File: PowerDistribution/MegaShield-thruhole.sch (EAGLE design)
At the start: 39 parts, among them IC1 TLE5205-2, IC2 TLE5205-2, IC3 TLE5205-2, J10 DCJ0202

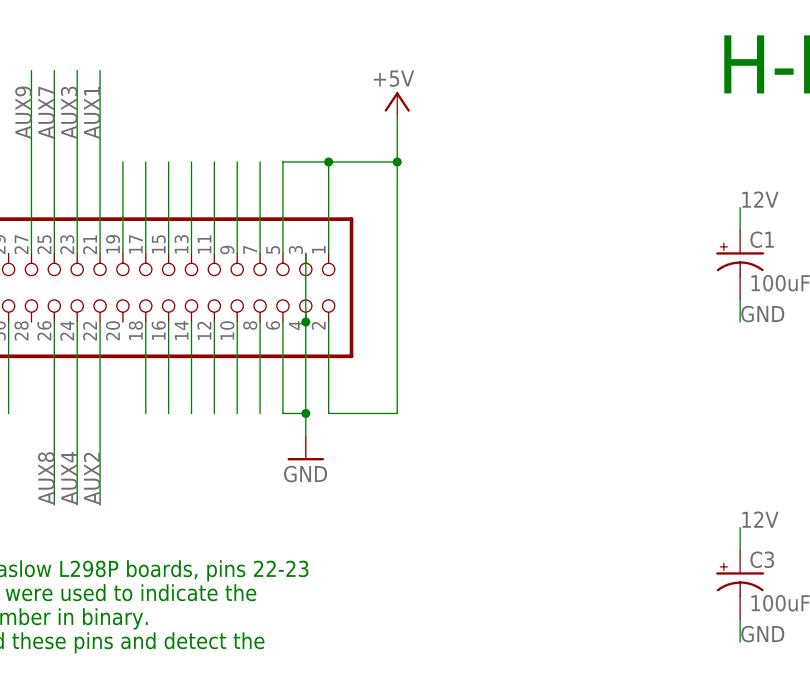
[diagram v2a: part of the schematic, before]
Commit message: Add second 5V bypass cap
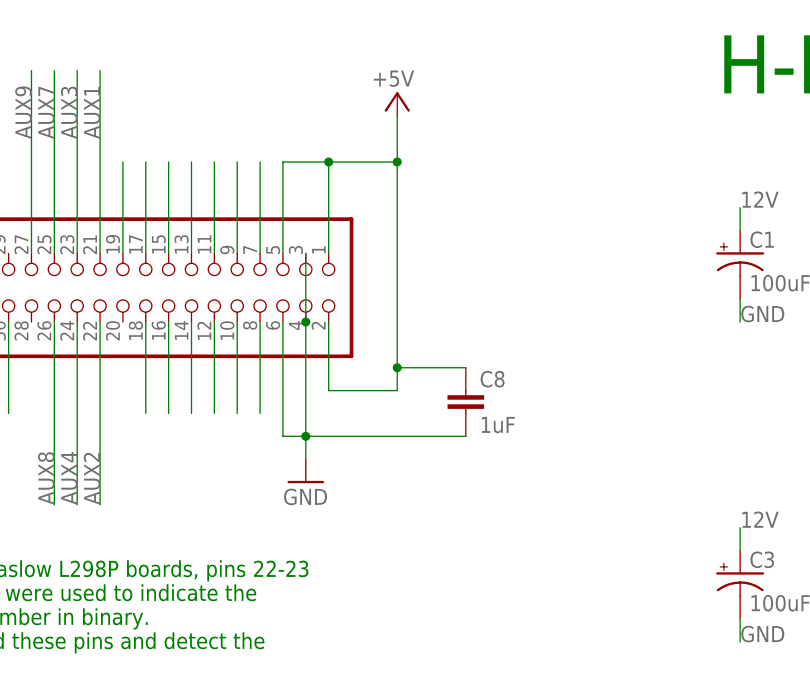
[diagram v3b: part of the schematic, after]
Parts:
- added C8: 1uF, SparkFun:CAPPTH
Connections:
- net 5V: now also C8.1
- net GND: now also C8.2
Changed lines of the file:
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@@
 <part name="GND2" library="supply1" deviceset="GND" device=""/>
 <part name="C7" library="SparkFun" deviceset="CAP" device="PTH" value="1uF"/>
+<part name="C8" library="SparkFun" deviceset="CAP" device="PTH" value="1uF"/>
 </parts>
 <sheets>
@@
 <attribute name="NAME" x="52.07" y="227.584" size="1.778" layer="95" rot="MR0"/>
 </instance>
-<instance part="GND1" gate="1" x="106.68" y="116.84" smashed="yes">
-<attribute name="VALUE" x="104.14" y="114.3" size="1.778" layer="96"/>
+<instance part="GND1" gate="1" x="106.68" y="114.3" smashed="yes">
+<attribute name="VALUE" x="104.14" y="111.76" size="1.778" layer="96"/>
 </instance>
 <instance part="TP1" gate="1" x="160.02" y="180.34"/>
@@
 </instance>
 <instance part="C7" gate="G$1" x="20.32" y="236.22" rot="MR0"/>
+<instance part="C8" gate="G$1" x="124.46" y="121.92"/>
 </instances>
 <busses>
@@
 <wire x1="106.68" y1="139.7" x2="106.68" y2="132.08" width="0.1524" layer="91"/>
 <pinref part="GND1" gate="1" pin="GND"/>
-<wire x1="106.68" y1="119.38" x2="106.68" y2="121.92" width="0.1524" layer="91"/>
-<wire x1="106.68" y1="132.08" x2="106.68" y2="121.92" width="0.1524" layer="91"/>
-<wire x1="106.68" y1="121.92" x2="104.14" y2="121.92" width="0.1524" layer="91"/>
+<wire x1="106.68" y1="116.84" x2="106.68" y2="119.38" width="0.1524" layer="91"/>
+<wire x1="106.68" y1="132.08" x2="106.68" y2="119.38" width="0.1524" layer="91"/>
+<wire x1="106.68" y1="119.38" x2="104.14" y2="119.38" width="0.1524" layer="91"/>
 <pinref part="XIO" gate="A" pin="6"/>
-<wire x1="104.14" y1="121.92" x2="104.14" y2="132.08" width="0.1524" layer="91"/>
-<junction x="106.68" y="121.92"/>
+<wire x1="104.14" y1="119.38" x2="104.14" y2="132.08" width="0.1524" layer="91"/>
+<junction x="106.68" y="119.38"/>
 <junction x="106.68" y="132.08"/>
+<pinref part="C8" gate="G$1" pin="2"/>
+<wire x1="106.68" y1="119.38" x2="124.46" y2="119.38" width="0.1524" layer="91"/>
 </segment>
 </net>
@@
 </segment>
 <segment>
-<wire x1="109.22" y1="132.08" x2="109.22" y2="121.92" width="0.1524" layer="91"/>
-<wire x1="109.22" y1="121.92" x2="116.84" y2="121.92" width="0.1524" layer="91"/>
-<wire x1="116.84" y1="121.92" x2="116.84" y2="149.86" width="0.1524" layer="91"/>
+<wire x1="109.22" y1="132.08" x2="109.22" y2="124.46" width="0.1524" layer="91"/>
+<wire x1="109.22" y1="124.46" x2="116.84" y2="124.46" width="0.1524" layer="91"/>
+<wire x1="116.84" y1="124.46" x2="116.84" y2="127" width="0.1524" layer="91"/>
+<wire x1="116.84" y1="127" x2="116.84" y2="149.86" width="0.1524" layer="91"/>
 <wire x1="116.84" y1="149.86" x2="109.22" y2="149.86" width="0.1524" layer="91"/>
 <wire x1="109.22" y1="149.86" x2="109.22" y2="139.7" width="0.1524" layer="91"/>
@@
 <wire x1="104.14" y1="149.86" x2="109.22" y2="149.86" width="0.1524" layer="91"/>
 <junction x="109.22" y="149.86"/>
-</segment>
-<segment>
+<pinref part="C8" gate="G$1" pin="1"/>
+<wire x1="124.46" y1="127" x2="116.84" y2="127" width="0.1524" layer="91"/>
+<junction x="116.84" y="127"/>
+</segment>
+<segment>

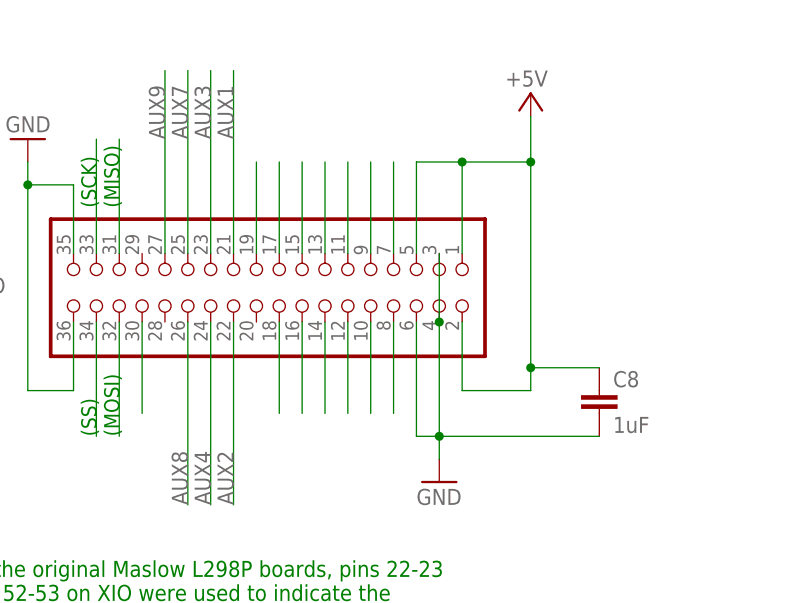
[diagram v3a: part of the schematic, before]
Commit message: Move caps on schematic, change colors in SMD .brd
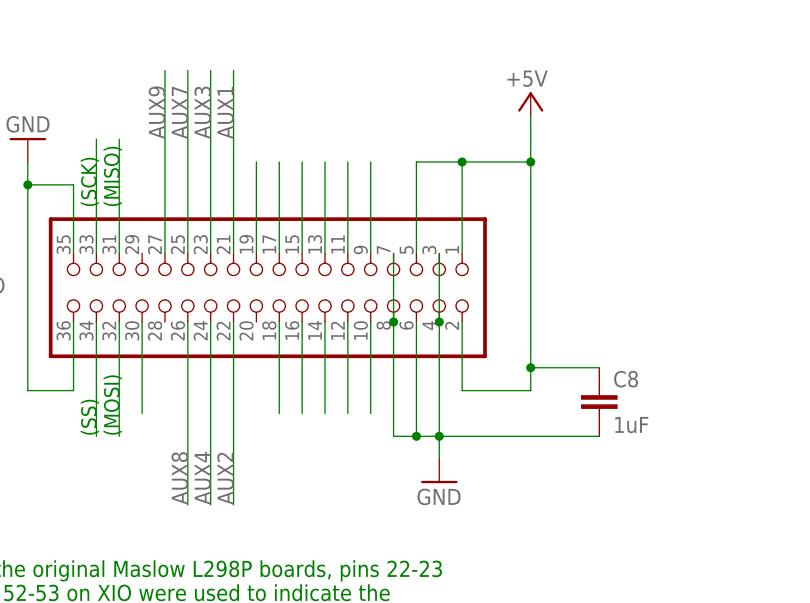
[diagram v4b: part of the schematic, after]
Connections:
- removed net PA4: XIO.7
- removed net PA5: XIO.8
- net GND: now also XIO.7, XIO.8
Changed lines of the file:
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@@
 <pinref part="C8" gate="G$1" pin="2"/>
 <wire x1="106.68" y1="119.38" x2="124.46" y2="119.38" width="0.1524" layer="91"/>
+<wire x1="101.6" y1="132.08" x2="101.6" y2="119.38" width="0.1524" layer="91"/>
+<pinref part="XIO" gate="A" pin="8"/>
+<wire x1="101.6" y1="119.38" x2="104.14" y2="119.38" width="0.1524" layer="91"/>
+<junction x="104.14" y="119.38"/>
+<wire x1="101.6" y1="139.7" x2="101.6" y2="132.08" width="0.1524" layer="91"/>
+<pinref part="XIO" gate="A" pin="7"/>
+<junction x="101.6" y="132.08"/>
 </segment>
 </net>
@@
 </segment>
 </net>
-<net name="PA4" class="0">
-<segment>
-<wire x1="101.6" y1="139.7" x2="101.6" y2="149.86" width="0.1524" layer="91"/>
-<pinref part="XIO" gate="A" pin="7"/>
-</segment>
-</net>
-<net name="PA5" class="0">
-<segment>
-<wire x1="101.6" y1="132.08" x2="101.6" y2="121.92" width="0.1524" layer="91"/>
-<pinref part="XIO" gate="A" pin="8"/>
-</segment>
-</net>
